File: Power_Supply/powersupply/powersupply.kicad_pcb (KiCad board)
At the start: 2 copper layers, 54 parts, among them J1 Conn_01x03, J2 USB_B_Micro, Q1 Q_PMOS_GDS, SW1 SW_Push, U1 AZ1117E-3.3, U10 MCP6001-OT, U2 ATSAMD10D13A-SS, U3 B0505S-2WR2, U4 TFT_OLED, U5 joystick-K1-1506DN-01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

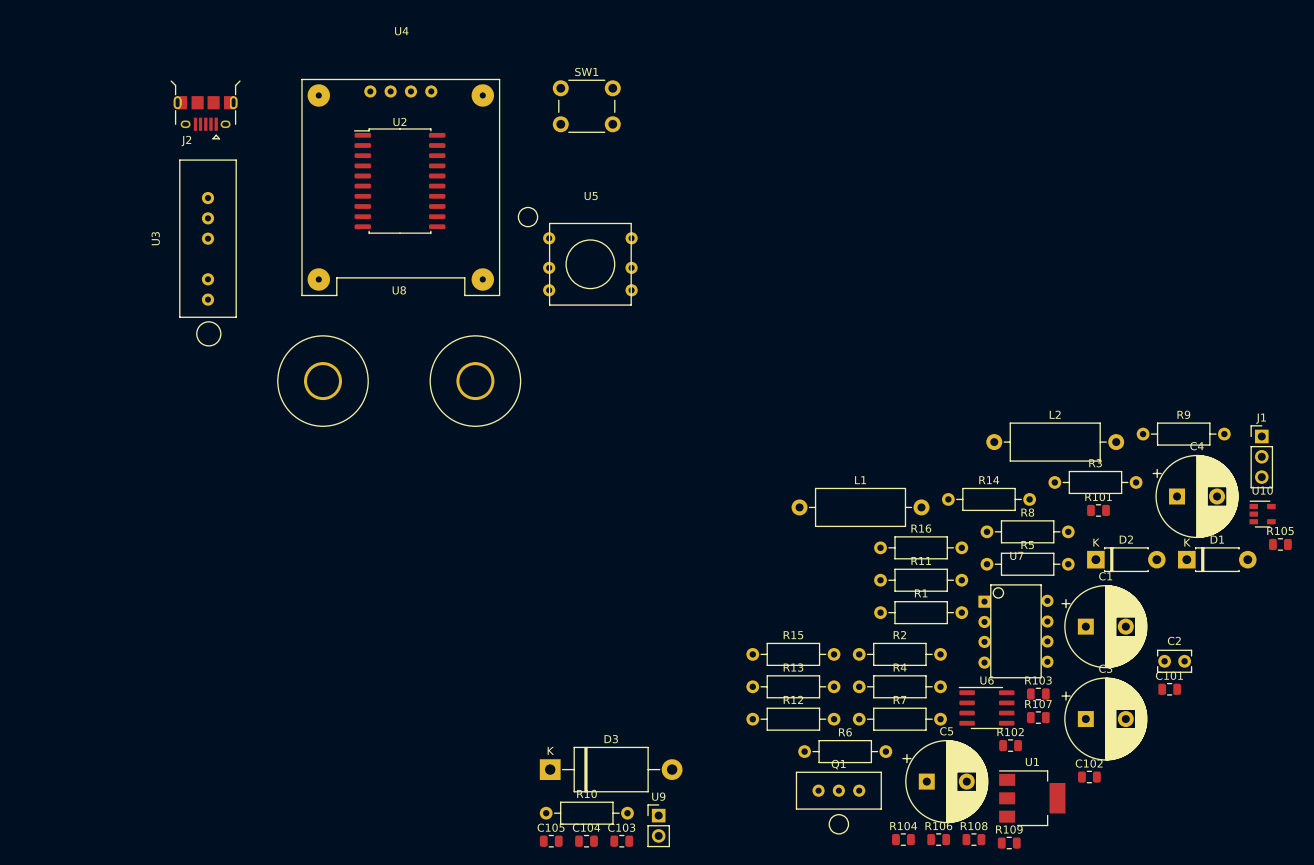
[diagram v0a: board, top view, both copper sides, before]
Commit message: Started layout
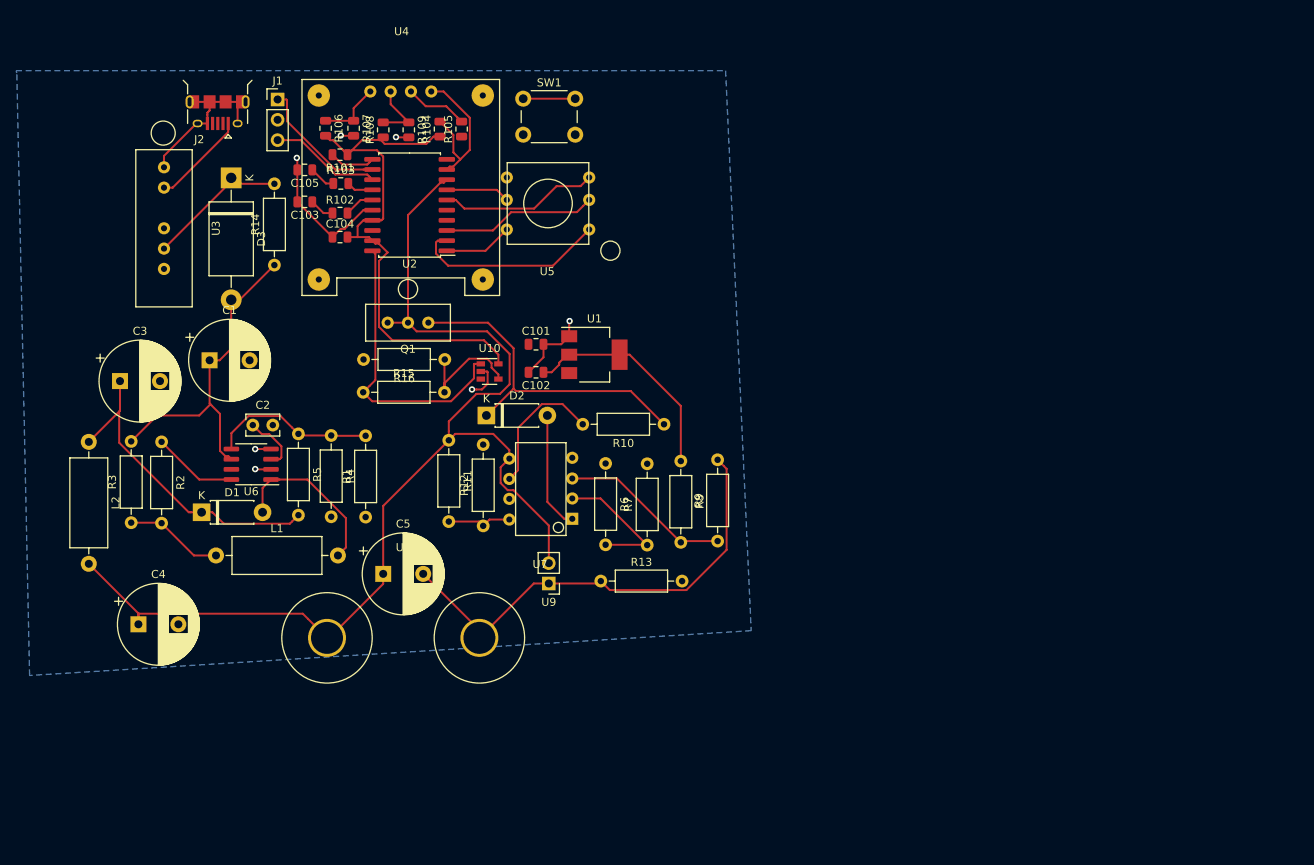
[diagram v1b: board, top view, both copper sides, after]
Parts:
- moved C4 130.8 mm to (55.3, 89.0)
- moved J1 130.0 mm to (72.7, 23.4)
- moved C3 127.9 mm to (53.0, 58.6)
- moved D1 123.3 mm to (63.2, 75.0)
- moved C2 117.7 mm to (69.6, 64.1)
- moved R106 117.4 mm to (78.7, 27.0), turned to 270 degrees
- moved R109 116.5 mm to (89.1, 27.2), turned to 270 degrees
- moved R3 115.6 mm to (54.4, 76.3), turned to 90 degrees
- moved R108 115.4 mm to (85.9, 27.2), turned to 90 degrees
- moved R105 114.8 mm to (95.7, 27.1), turned to 90 degrees
- moved C1 114.5 mm to (64.2, 56.0)
- moved L2 113.2 mm to (49.1, 66.2), turned to 270 degrees
- moved R107 112.9 mm to (82.2, 27.0), turned to 270 degrees
- moved R103 108.1 mm to (80.6, 33.9)
- moved R102 107.0 mm to (80.5, 37.6)
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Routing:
- net /Boost_out: track 0.00 -> 146.3 mm
- net +3V3: track 0.00 -> 96.1 mm
- net /V_negative_out: track 0.00 -> 59.0 mm
- net Net-(D2-Pad1): track 0.00 -> 42.5 mm
- net +5V: track 0.00 -> 42.3 mm
- net Net-(C3-Pad1): track 0.00 -> 40.2 mm
- net GND: track 0.00 -> 39.9 mm, vias 0 -> 7
- net /V_current_amplified: track 0.00 -> 36.6 mm
- net /up: track 0.00 -> 24.5 mm
- net Net-(R8-Pad2): track 0.00 -> 21.5 mm
- net Net-(D1-Pad2): track 0.00 -> 21.0 mm
- net Net-(R1-Pad2): track 0.00 -> 20.7 mm
- net Net-(J2-Pad5): track 0.00 -> 20.0 mm
- net /SDA: track 0.00 -> 19.9 mm
- net /down: track 0.00 -> 19.9 mm
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- added copper zone on B.Cu, net GND

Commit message: layout changes
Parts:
- moved U10 25.1 mm to (75.1, 50.2), turned to 180 degrees
- moved U1 22.4 mm to (89.9, 54.9), turned to 270 degrees
- moved R16 20.3 mm to (73.7, 59.5), turned to 0 degrees
- moved C101 17.0 mm to (89.0, 48.2), turned to 90 degrees
- moved C102 16.2 mm to (91.8, 48.1), turned to 270 degrees
- moved Q1 16.1 mm to (104.1, 56.6)
- moved R1 12.6 mm to (85.6, 63.1), turned to 180 degrees
- moved D1 10.3 mm to (71.9, 80.4)
- moved C4 7.48 mm to (59.5, 82.8)
- moved C5 5.59 mm to (91.5, 82.7), turned to 180 degrees
- moved R5 5.57 mm to (75.4, 70.8), turned to 0 degrees
- moved R2 5.24 mm to (62.7, 63.6)
- moved R3 5.24 mm to (58.9, 73.7)
- moved L1 5.17 mm to (66.9, 75.6)
- moved L2 4.88 mm to (53.3, 63.7)
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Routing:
- net /V_negative_out: track 59.0 -> 137.0 mm, vias 0 -> 2
- net /V_lin_ctrl: track 0.00 -> 51.0 mm
- net +3V3: track 96.1 -> 122.2 mm, vias 0 -> 2
- net Net-(C3-Pad1): track 40.2 -> 62.4 mm
- net +5V: track 42.3 -> 60.0 mm, vias 0 -> 2
- net /V_current_amplified: track 36.6 -> 22.6 mm
- net Net-(D2-Pad1): track 42.5 -> 32.8 mm
- net /Boost_out: track 146.3 -> 137.4 mm, vias 0 -> 2
- net GND: track 39.9 -> 46.3 mm
- net Net-(L1-Pad1): track 12.3 -> 17.0 mm
- net Net-(D1-Pad2): track 21.0 -> 18.1 mm
- net Net-(R15-Pad2): track 15.0 -> 13.3 mm
- net Net-(R2-Pad1): track 10.7 -> 9.72 mm

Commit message: more layout
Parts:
- moved R7 36.9 mm to (98.0, 48.7), turned to 0 degrees
- moved R8 34.6 mm to (89.5, 60.5), turned to 0 degrees
- moved R9 31.2 mm to (99.8, 64.7), turned to 180 degrees
- moved R13 27.6 mm to (89.7, 69.0)
- moved C5 26.9 mm to (65.0, 87.2), turned to 0 degrees
- moved R6 24.7 mm to (108.0, 44.9), turned to 180 degrees
- moved R10 20.9 mm to (103.8, 76.0), turned to 90 degrees
- moved Q1 20.7 mm to (96.5, 75.9), turned to 90 degrees
- moved D2 18.7 mm to (90.5, 79.7), turned to 90 degrees
- moved R11 17.8 mm to (111.8, 66.0)
- moved U7 14.0 mm to (107.0, 58.2), turned to 0 degrees
- moved D1 13.8 mm to (58.1, 80.0)
- moved J1 12.5 mm to (62.0, 29.9), turned to 90 degrees
- moved R15 11.1 mm to (73.6, 59.6), turned to 0 degrees
- moved R16 10.9 mm to (83.9, 55.7), turned to 180 degrees
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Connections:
- C5 pad 1: /Boost_out -> /V_positive_out
- Q1 pad 2: /Boost_out -> /V_positive_out
- R11 pad 1: /Boost_out -> /V_positive_out
- R6 pad 1: /Vlim -> /V_lin_ctrl
- U2 pad 8: /Boost_out -> /V_positive_out
- U8 pad 2: /Boost_out -> /V_positive_out
- U9 pad 2: /Boost_out -> /V_positive_out
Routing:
- net /V_positive_out: track 0.00 -> 157.3 mm
- net /Boost_out: track 137.4 -> 78.3 mm, vias 2 -> 0
- net /V_negative_out: track 137.0 -> 83.2 mm
- net +3V3: track 122.2 -> 81.4 mm, vias 2 -> 0
- net Net-(R101-Pad2): track 12.3 -> 35.6 mm, vias 0 -> 2
- net Net-(R11-Pad2): track 8.12 -> 27.2 mm
- net Net-(D2-Pad1): track 32.8 -> 14.8 mm
- net Net-(R8-Pad2): track 21.5 -> 8.38 mm
- net GND: track 46.3 -> 37.1 mm
- net Net-(D2-Pad2): track 14.8 -> 23.3 mm
- net Net-(R10-Pad2): track 17.2 -> 9.75 mm
- net /right: track 8.02 -> 14.4 mm
- net Net-(D1-Pad2): track 18.1 -> 23.9 mm
- net /V_lin_ctrl: track 51.0 -> 47.0 mm
- net /SWCLK: track 17.0 -> 20.8 mm
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
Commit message: even more layout
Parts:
- added H1: MountingHole, MountingHole:MountingHole_3.2mm_M3, F.Cu at (49.2, 89.0)
- added H2: MountingHole, MountingHole:MountingHole_3.2mm_M3, F.Cu at (114.3, 24.9)
- added H3: MountingHole, MountingHole:MountingHole_3.2mm_M3, F.Cu at (114.3, 88.7)
- added H4: MountingHole, MountingHole:MountingHole_3.2mm_M3, F.Cu at (49.2, 24.8)
- added TP1: Boost_out, Connector_PinSocket_2.54mm:PinSocket_1x01_P2.54mm_Vertical, F.Cu at (77.3, 80.8)
- added TP2: +5_isolated, Connector_PinSocket_2.54mm:PinSocket_1x01_P2.54mm_Vertical, F.Cu at (79.5, 51.4)
- added TP3: +3.3, Connector_PinSocket_2.54mm:PinSocket_1x01_P2.54mm_Vertical, F.Cu at (97.8, 56.7)
- added TP4: Current_limit, Connector_PinSocket_2.54mm:PinSocket_1x01_P2.54mm_Vertical, F.Cu at (97.0, 47.8)
- added TP5: Voltage_limit, Connector_PinSocket_2.54mm:PinSocket_1x01_P2.54mm_Vertical, F.Cu at (108.5, 79.4)
- added TP6: Boost_ctrl, Connector_PinSocket_2.54mm:PinSocket_1x01_P2.54mm_Vertical, F.Cu at (66.3, 46.0)
- added TP7: GND, Connector_PinSocket_2.54mm:PinSocket_1x01_P2.54mm_Vertical, F.Cu at (53.3, 83.3)
- moved U9 12.4 mm to (101.6, 79.4), turned to 90 degrees
- moved C4 5.48 mm to (58.4, 87.8)
- moved C5 4.70 mm to (69.6, 87.8)
- moved J2 4.61 mm to (62.9, 20.7)
- moved R14 4.29 mm to (66.3, 41.9)
- moved U8 3.83 mm to (93.2, 87.7)
- moved R6 3.37 mm to (111.4, 45.4)
- moved R7 3.23 mm to (101.2, 48.9)
- moved J1 2.63 mm to (60.3, 27.9)
- moved U1 2.05 mm to (90.9, 53.8)
- moved D3 1.86 mm to (60.6, 32.3)
- moved U4 1.85 mm to (81.5, 34.5)
- moved C105 1.73 mm to (71.3, 34.0)
- moved Q1 1.69 mm to (96.0, 77.5)
- moved D2 1.68 mm to (90.5, 81.3)
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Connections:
- net Net-(R11-Pad2) renamed /Voltage_limit_divider
- net Net-(R6-Pad2) renamed /Current_limit_divider
- R1 pad 1: /Vref -> /V_boost_ctrl
- R6 pad 1: /V_lin_ctrl -> /V_curr_lim
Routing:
- net /V_boost_ctrl: track 3.33 -> 69.2 mm
- net /V_curr_lim: track 3.10 -> 46.8 mm, vias 0 -> 2
- net +5V: track 60.7 -> 72.1 mm
- net +3V3: track 81.4 -> 91.4 mm
- net /V_positive_out: track 157.3 -> 148.7 mm
- net Net-(J2-Pad1): track 11.2 -> 19.2 mm
- net Net-(J2-Pad5): track 19.8 -> 26.7 mm
- net /Voltage_limit_divider: track 27.2 -> 31.5 mm
- net /V_lin_ctrl: track 47.0 -> 43.1 mm
- net /SWDIO: track 14.1 -> 17.1 mm
- net /Current_limit_divider: track 16.0 -> 18.8 mm
- net /SWCLK: track 20.8 -> 23.6 mm
- net Net-(R15-Pad2): track 14.5 -> 16.6 mm
- net /V_negative_out: track 83.2 -> 81.5 mm
- net Net-(C2-Pad1): track 7.46 -> 5.84 mm
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
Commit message: edge-cuts svg
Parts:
- moved TP3 1.27 mm to (98.1, 55.5)
- moved R101 0.64 mm to (75.7, 31.0), turned to 0 degrees
- moved R103 0.14 mm to (75.7, 34.1)
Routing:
- net Net-(R101-Pad2): track 35.6 -> 32.9 mm
- net +3V3: track 91.4 -> 93.4 mm
- net /SWCLK: track 23.6 -> 22.9 mm

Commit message: almost finished layout
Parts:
- moved SW1 18.2 mm to (114.7, 33.6), turned to 270 degrees
- moved H1 2.32 mm to (50.9, 90.6)
- moved H3 2.25 mm to (113.1, 90.6)
- moved U9 2.03 mm to (103.7, 79.4), turned to 270 degrees
- moved U5 1.81 mm to (101.4, 36.3)
- moved TP3 1.18 mm to (99.2, 55.9)
- moved TP7 0.68 mm to (53.2, 84.0)
- moved TP6 0.30 mm to (66.3, 45.7)
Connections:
- U8 pad 1: /V_negative_out -> /V_positive_out
- U8 pad 2: /V_positive_out -> /V_negative_out
- U9 pad 1: /V_negative_out -> /V_positive_out
- U9 pad 2: /V_positive_out -> /V_negative_out
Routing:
- net Net-(R101-Pad2): track 32.9 -> 46.8 mm
- net /right: track 14.4 -> 9.29 mm
- net /V_positive_out: track 148.7 -> 146.5 mm
- net /center: track 9.95 -> 8.33 mm
- net /up: track 25.7 -> 24.1 mm
- net /left: track 20.7 -> 19.1 mm
- net +3V3: track 93.4 -> 94.5 mm
- net /down: track 21.7 -> 21.0 mm
- net /V_negative_out: track 81.5 -> 82.1 mm
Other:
- board outline added: 62.2 x 0.2 mm
- board text added: "+"
- board text added: "+3.3V"
- board text added: "+5V I"
- board text added: "-"
- board text added: "- +"
- board text added: "Boost Control"
- board text added: "Boost Out"
- board text added: "Current Limit"
- board text added: "GND"
- board text added: "Power Supply"
- board text added: "Reset"
- board text added: "Voltage Limit"

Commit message: check
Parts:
- moved H2 2.39 mm to (114.0, 22.5)
- moved H4 2.37 mm to (50.0, 22.5)
- moved H3 1.10 mm to (114.0, 90.0)
- moved H1 1.08 mm to (50.0, 90.0)
- moved J2 0.15 mm to (62.9, 20.6)
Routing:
- net Net-(J2-Pad1): track 19.2 -> 20.6 mm
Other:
- board size 62.2 x 0.2 mm -> 70.9 x 74.5 mm
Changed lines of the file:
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@@
   (general
     (thickness 1.6)
-    (drawings 13)
-    (tracks 417)
+    (drawings 18)
+    (tracks 419)
     (zones 0)
     (modules 65)
@@
     (mod_text_size 1 1)
     (mod_text_width 0.15)
-    (pad_size 1.524 1.524)
-    (pad_drill 0.762)
+    (pad_size 3.2 3.2)
+    (pad_drill 3.2)
     (pad_to_mask_clearance 0.051)
     (solder_mask_min_width 0.25)
@@
   )
   (module MountingHole:MountingHole_3.2mm_M3 (layer F.Cu)
-    (at 49.25 24.75)
+    (at 50 22.5)
     (descr "Mounting Hole 3.2mm, no annular, M3")
     (tags "mounting hole 3.2mm no annular m3")
@@
   )
   (module MountingHole:MountingHole_3.2mm_M3 (layer F.Cu)
-    (at 113.075 90.6)
+    (at 114 90)
     (descr "Mounting Hole 3.2mm, no annular, M3")
     (tags "mounting hole 3.2mm no annular m3")
@@
   )
   (module MountingHole:MountingHole_3.2mm_M3 (layer F.Cu)
-    (at 114.275 24.875)
+    (at 114 22.5)
     (descr "Mounting Hole 3.2mm, no annular, M3")
     (tags "mounting hole 3.2mm no annular m3")
@@
   )
   (module MountingHole:MountingHole_3.2mm_M3 (layer F.Cu)
-    (at 50.9 90.6)
+    (at 50 90)
     (descr "Mounting Hole 3.2mm, no annular, M3")
     (tags "mounting hole 3.2mm no annular m3")
@@
     (descr https://www.omron.com/ecb/products/pdf/en-b3f.pdf)
     (tags "tact sw push 6mm")
-    (fp_text reference SW1 (at 3.2232 -2.4986 90) (layer F.SilkS)
+    (fp_text reference SW1 (at 9.0978 -0.2354 180) (layer F.SilkS)
       (effects (font (size 1 1) (thickness 0.15)))
     )
@@
   )
   (module powersupply:USB_Micro-B_Amphenol_10118194-0001LF_Horizontal (layer F.Cu)
-    (at 62.85 20.725 180)
+    (at 62.85 20.5726 180)
     (tags "USB USB_B USB_micro USB_OTG")
     (attr smd)
@@
     )
   )
-  (gr_line (start 113.125 94.25) (end 50.9 94.05) (layer Edge.Cuts) (width 0.05))
+  (gr_line (start 113.9952 19.05) (end 113.9952 18.9992) (layer Edge.Cuts) (width 0.05))
+  (gr_line (start 50 19.05) (end 114 19.05) (layer Edge.Cuts) (width 0.05))
+  (gr_line (start 46.55 22.5) (end 46.55 90) (layer Edge.Cuts) (width 0.05))
+  (gr_line (start 117.1448 93.0148) (end 117.0432 92.71) (layer Edge.Cuts) (width 0.05))
+  (gr_line (start 117.45 22.5) (end 117.45 90) (layer Edge.Cuts) (width 0.05))
+  (gr_line (start 114 93.45) (end 50 93.45) (layer Edge.Cuts) (width 0.05))
   (gr_text "Power\nSupply" (at 103.2 24.65) (layer F.SilkS)
     (effects (font (size 2.3 2.3) (thickness 0.3)))
@@
   (segment (start 79.5954 32.3596) (end 73.63242 32.3596) (width 0.25) (layer F.Cu) (net 15))
   (segment (start 79.75 32.205) (end 79.5954 32.3596) (width 0.25) (layer F.Cu) (net 15))
-  (segment (start 59.95 20.725) (end 65.75 20.725) (width 0.25) (layer F.Cu) (net 16))
-  (segment (start 61.575 22.35) (end 61.575 23.425) (width 0.25) (layer F.Cu) (net 16))
-  (segment (start 61.575 22.075) (end 61.575 22.35) (width 0.25) (layer F.Cu) (net 16))
-  (segment (start 61.85 21.8) (end 61.575 22.075) (width 0.25) (layer F.Cu) (net 16))
-  (segment (start 61.85 20.725) (end 61.85 21.8) (width 0.25) (layer F.Cu) (net 16))
-  (segment (start 61.575 23.425) (end 60.35 23.425) (width 0.25) (layer F.Cu) (net 16))
-  (segment (start 65.35 21.125) (end 65.75 20.725) (width 0.25) (layer F.Cu) (net 16))
-  (segment (start 65.35 23.425) (end 65.35 21.125) (width 0.25) (layer F.Cu) (net 16))
-  (segment (start 60.35 23.425) (end 60.2 23.425) (width 0.25) (layer F.Cu) (net 16))
-  (segment (start 56.875 23.425) (end 60.35 23.425) (width 0.25) (layer F.Cu) (net 16))
+  (segment (start 59.95 20.5726) (end 65.75 20.5726) (width 0.25) (layer F.Cu) (net 16))
+  (segment (start 61.575 22.1976) (end 61.575 23.2726) (width 0.25) (layer F.Cu) (net 16))
+  (segment (start 61.575 21.9226) (end 61.575 22.1976) (width 0.25) (layer F.Cu) (net 16))
+  (segment (start 61.85 21.6476) (end 61.575 21.9226) (width 0.25) (layer F.Cu) (net 16))
+  (segment (start 61.85 20.5726) (end 61.85 21.6476) (width 0.25) (layer F.Cu) (net 16))
+  (segment (start 61.575 23.2726) (end 60.35 23.2726) (width 0.25) (layer F.Cu) (net 16))
+  (segment (start 65.35 20.9726) (end 65.75 20.5726) (width 0.25) (layer F.Cu) (net 16))
+  (segment (start 65.35 23.2726) (end 65.35 20.9726) (width 0.25) (layer F.Cu) (net 16))
+  (segment (start 60.35 23.2726) (end 60.2 23.2726) (width 0.25) (layer F.Cu) (net 16))
   (segment (start 53.575 26.725) (end 56.875 23.425) (width 0.25) (layer F.Cu) (net 16))
   (segment (start 53.575 32.405) (end 53.575 26.725) (width 0.25) (layer F.Cu) (net 16))
-  (segment (start 54.336999 34.183001) (end 53.575 34.945) (width 0.25) (layer F.Cu) (net 17))
-  (segment (start 55.625 32.895) (end 54.336999 34.183001) (width 0.25) (layer F.Cu) (net 17))
-  (segment (start 55.625 27.425) (end 55.625 32.895) (width 0.25) (layer F.Cu) (net 17))
-  (segment (start 63.225 25.45) (end 57.6 25.45) (width 0.25) (layer F.Cu) (net 17))
-  (segment (start 57.6 25.45) (end 55.625 27.425) (width 0.25) (layer F.Cu) (net 17))
-  (segment (start 64.175 24.5) (end 63.225 25.45) (width 0.25) (layer F.Cu) (net 17))
-  (segment (start 64.175 23.425) (end 64.175 24.5) (width 0.25) (layer F.Cu) (net 17))
+  (segment (start 59.239 23.425) (end 59.3914 23.2726) (width 0.25) (layer F.Cu) (net 16))
+  (segment (start 56.875 23.425) (end 59.239 23.425) (width 0.25) (layer F.Cu) (net 16))
+  (segment (start 59.3914 23.2726) (end 60.35 23.2726) (width 0.25) (layer F.Cu) (net 16))
+  (segment (start 64.175 23.2726) (end 64.175 24.3476) (width 0.25) (layer F.Cu) (net 17))
+  (segment (start 64.175 24.7758) (end 64.175 23.2726) (width 0.25) (layer F.Cu) (net 17))
+  (segment (start 63.5008 25.45) (end 64.175 24.7758) (width 0.25) (layer F.Cu) (net 17))
+  (segment (start 55.625 27.425) (end 57.6 25.45) (width 0.25) (layer F.Cu) (net 17))
+  (segment (start 55.625 32.895) (end 55.625 27.425) (width 0.25) (layer F.Cu) (net 17))
+  (segment (start 57.6 25.45) (end 63.5008 25.45) (width 0.25) (layer F.Cu) (net 17))
+  (segment (start 53.575 34.945) (end 55.625 32.895) (width 0.25) (layer F.Cu) (net 17))
   (segment (start 62.6612 73.6584) (end 62.7212 73.7184) (width 0.25) (layer F.Cu) (net 21))
   (segment (start 58.9212 73.6584) (end 62.6612 73.6584) (width 0.25) (layer F.Cu) (net 21))
@@
     (polygon
       (pts
-        (xy 45.15 19.275) (xy 118.925 19.45) (xy 118.85 93.85) (xy 45.125 94.075)
+        (xy 45.15 19.275) (xy 117.6903 19.6452) (xy 117.6153 94.0452) (xy 45.125 94.075)
       )
     )

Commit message: finalish changes
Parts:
- removed R106, R107, R108, R109: 0, Resistor_SMD:R_0805_2012Metric
- added R17: 10k, Resistor_THT:R_Axial_DIN0207_L6.3mm_D2.5mm_P10.16mm_Horizontal, F.Cu at (101.1, 41.8)
- added TP10: TestPoint, TestPoint:TestPoint_Pad_1.5x1.5mm, F.Cu at (82.7, 26.9)
- added TP11: TestPoint, TestPoint:TestPoint_Pad_1.5x1.5mm, F.Cu at (79.3, 26.9)
- added TP8: TestPoint, TestPoint:TestPoint_Pad_1.5x1.5mm, F.Cu at (72.9, 26.9)
- added TP9: TestPoint, TestPoint:TestPoint_Pad_1.5x1.5mm, F.Cu at (76.1, 26.9)
- C1: value 330uF -> 470uF; footprint Capacitor_THT:CP_Radial_D10.0mm_P5.00mm -> Capacitor_THT:CP_Radial_D8.0mm_P3.50mm
- C2: value 1500pF -> 270pF
- C3: value 330uF -> 470u
- C4: value 100uF -> 470u
- L1: value 170uH -> 47uH; footprint Inductor_THT:L_Axial_L11.0mm_D4.5mm_P15.24mm_Horizontal_Fastron_MECC -> Inductor_THT:L_Radial_D8.7mm_P5.00mm_Fastron_07HCP
- R3: value 0.22 -> 0.3 1/4W
- R8: value 132k -> 10k
- moved D3 15.0 mm to (61.0, 47.3), turned to 90 degrees
- moved R14 9.85 mm to (66.1, 32.1), turned to 270 degrees
- moved TP1 6.32 mm to (81.6, 76.2)
- moved L1 4.32 mm to (70.8, 77.5)
- moved SW1 4.01 mm to (114.5, 29.6)
- moved U5 3.43 mm to (101.8, 32.9)
- moved R104 2.18 mm to (89.4, 26.6)
- moved R105 2.18 mm to (85.7, 26.6)
- moved R101 0.36 mm to (75.7, 30.6)
- moved C105 0.11 mm to (71.3, 34.1)
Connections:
- D3 pad 1: Net-(D3-Pad1) -> +5V
- D3 pad 2: +5V -> GND
- R105 pad 2: Net-(R105-Pad2) -> /SCK
- R14 pad 1: +5V -> GND
- R14 pad 2: Net-(D3-Pad1) -> +5V
- U10 pad 3: /V_negative_out -> Net-(R8-Pad2)
- U3 pad 4: Net-(D3-Pad1) -> +5V
- U4 pad 1: Net-(R106-Pad1) -> GND
- U4 pad 2: Net-(R108-Pad2) -> +3V3
- U4 pad 3: Net-(R105-Pad2) -> /SCK
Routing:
- net Net-(R8-Pad2): track 8.38 -> 39.4 mm
- net +3V3: track 94.5 -> 121.5 mm
- net /SCK: track 0.00 -> 25.6 mm
- net /V_negative_out: track 82.1 -> 61.8 mm
- net Net-(D3-Pad1): track 19.3 -> 0.00 mm
- net /V_lin_ctrl: track 43.1 -> 61.2 mm
- net /Current_limit_divider: track 18.8 -> 30.4 mm
- net /V_curr_lim: track 46.8 -> 57.8 mm
- net +5V: track 72.1 -> 80.8 mm
- net Net-(R106-Pad1): track 7.44 -> 0.00 mm
- net Net-(R108-Pad2): track 7.33 -> 0.00 mm
- net Net-(R105-Pad2): track 7.06 -> 0.00 mm
- net GND: track 37.6 -> 44.3 mm, vias 7 -> 6
- net Net-(L1-Pad1): track 17.0 -> 23.5 mm
- net /V_positive_out: track 146.5 -> 151.6 mm
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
